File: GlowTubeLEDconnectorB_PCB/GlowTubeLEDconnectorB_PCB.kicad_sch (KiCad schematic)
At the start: 2 parts, among them U1 Contact pads, U2 Contact pads

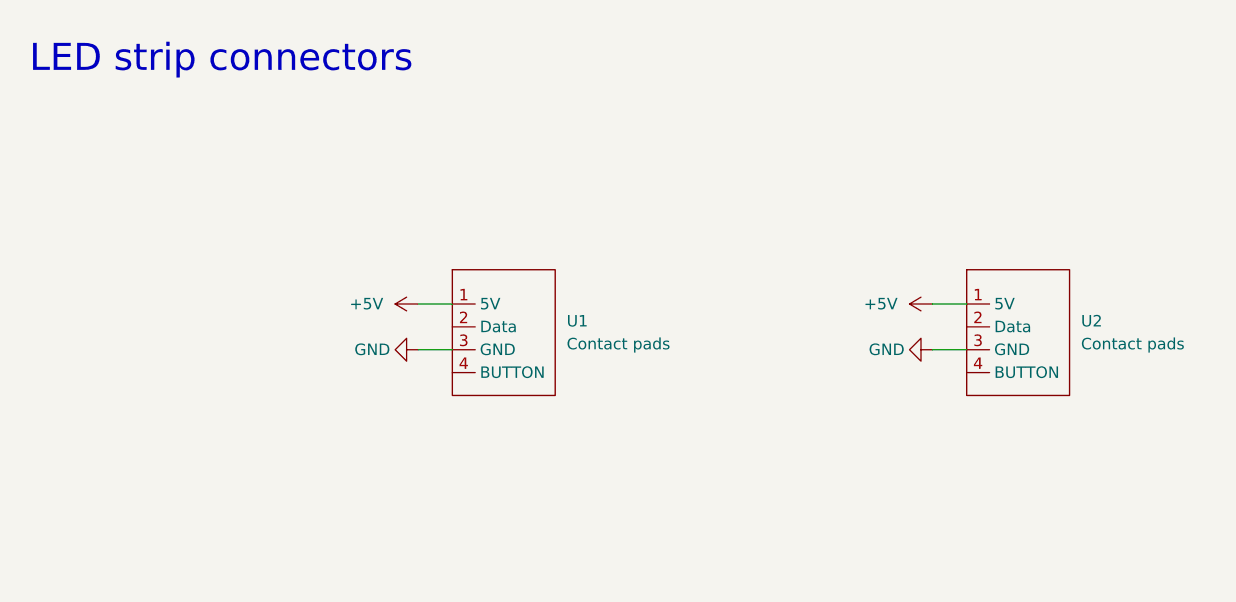
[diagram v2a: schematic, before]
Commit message: updated PCB designs to release candidate 1
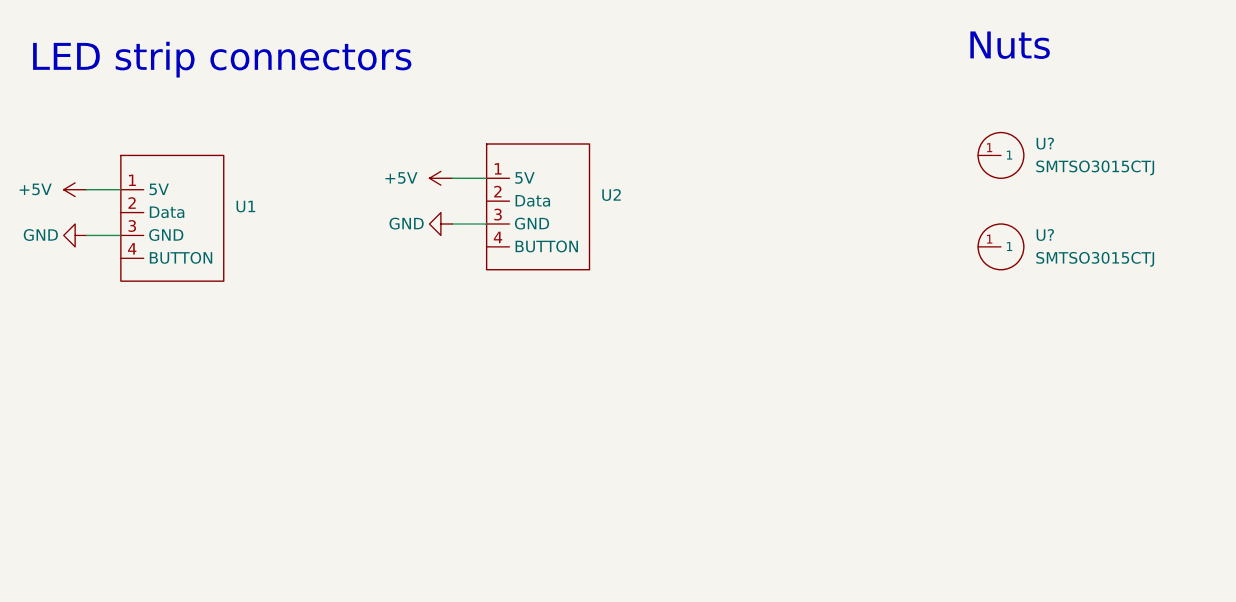
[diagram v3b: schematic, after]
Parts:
- added U? (x2): SMTSO3015CTJ, footprint:SMTSO3030CTJ, symbol MyParts:SMTSO3015CTJ
- U1, U2: value Contact pads -> (none); footprint myparts:LED strip connector 4pad small -> (none); now left out of the parts list
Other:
- note added: "Nuts"
- moved on the sheet: U1, U2
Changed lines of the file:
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@@
 (kicad_sch (version 20211123) (generator eeschema)
   (paper "A5")
-  (wire (pts (xy 64.77 52.07) (xy 68.58 52.07))
+  (wire (pts (xy 27.94 39.37) (xy 31.75 39.37))
     (stroke (width 0) (type default) (color 0 0 0 0))
   )
-  (wire (pts (xy 121.92 57.15) (xy 125.73 57.15))
+  (wire (pts (xy 68.58 43.18) (xy 72.39 43.18))
     (stroke (width 0) (type default) (color 0 0 0 0))
   )
-  (wire (pts (xy 121.92 52.07) (xy 125.73 52.07))
+  (wire (pts (xy 68.58 38.1) (xy 72.39 38.1))
     (stroke (width 0) (type default) (color 0 0 0 0))
   )
-  (wire (pts (xy 64.77 57.15) (xy 68.58 57.15))
+  (wire (pts (xy 27.94 44.45) (xy 31.75 44.45))
     (stroke (width 0) (type default) (color 0 0 0 0))
+  )
+  (text "Nuts" (at 125.73 25.4 0)
+    (effects (font (size 3 3)) (justify left bottom))
   )
   (text "LED strip connectors" (at 21.59 26.67 0)
     (effects (font (size 3 3)) (justify left bottom))
   )
-  (symbol (lib_id "myparts:LED_strip_contact_4pads") (at 72.39 52.07 0) (unit 1)
-    (in_bom yes) (on_board yes) (fields_autoplaced)
-    (property "Reference" "U1" (id 0) (at 81.28 53.9749 0)
+  (symbol (lib_id "myparts:LED_strip_contact_4pads") (at 35.56 39.37 0) (unit 1)
+    (in_bom no) (on_board yes) (fields_autoplaced)
+    (property "Reference" "U1" (id 0) (at 44.45 41.2749 0)
       (effects (font (size 1.27 1.27)) (justify left))
     )
-    (property "Value" "Contact pads" (id 1) (at 81.28 56.5149 0)
+    (property "Value" "" (id 1) (at 44.45 43.8149 0)
       (effects (font (size 1.27 1.27)) (justify left))
     )
-    (property "Footprint" "myparts:LED strip connector 4pad small" (id 2) (at 72.39 52.07 0)
+    (property "Footprint" "" (id 2) (at 35.56 39.37 0)
       (effects (font (size 1.27 1.27)) hide)
     )
-    (property "Datasheet" "" (id 3) (at 72.39 52.07 0)
+    (property "Datasheet" "" (id 3) (at 35.56 39.37 0)
       (effects (font (size 1.27 1.27)) hide)
     )
@@
     (pin "4")
   )
-  (symbol (lib_id "power:GND") (at 121.92 57.15 270) (unit 1)
-    (in_bom yes) (on_board yes)
-    (property "Reference" "#PWR0103" (id 0) (at 115.57 57.15 0)
-      (effects (font (size 1.27 1.27)) hide)
+  (symbol (lib_id "MyParts:SMTSO3015CTJ") (at 129.54 39.37 0) (unit 1)
+    (in_bom yes) (on_board yes) (fields_autoplaced)
+    (property "Reference" "U?" (id 0) (at 133.35 44.4499 0)
+      (effects (font (size 1.27 1.27)) (justify left))
     )
-    (property "Value" "GND" (id 1) (at 116.84 57.15 90))
-    (property "Footprint" "" (id 2) (at 121.92 57.15 0)
-      (effects (font (size 1.27 1.27)) hide)
+    (property "Value" "SMTSO3015CTJ" (id 1) (at 133.35 46.9899 0)
+      (effects (font (size 1.27 1.27)) (justify left))
     )
-    (property "Datasheet" "" (id 3) (at 121.92 57.15 0)
+    (property "Footprint" "footprint:SMTSO3030CTJ" (id 2) (at 129.54 49.53 0)
+      (effects (font (size 1.27 1.27) italic) hide)
+    )
+    (property "Datasheet" "https://img.jlc.com/pdf/applyPasteComponent/2021-07-26/212394W/84600014a36a49d2b26ab413315c8aa0/SINHOO%E7%94%B5%E8%B7%AF%E6%9D%BF%E8%A1%A8%E8%B4%B4%E8%9E%BA%E6%AF%8D%E6%9F%B1PCBSMDNuts.pdf" (id 3) (at 127.254 39.243 0)
+      (effects (font (size 1.27 1.27)) (justify left) hide)
+    )
+    (property "LCSC #" "C2915308" (id 4) (at 129.54 39.37 0)
       (effects (font (size 1.27 1.27)) hide)
     )
     (pin "1")
   )
-  (symbol (lib_id "power:+5V") (at 121.92 52.07 90) (unit 1)
+  (symbol (lib_id "power:GND") (at 68.58 43.18 270) (unit 1)
     (in_bom yes) (on_board yes)
-    (property "Reference" "#PWR0104" (id 0) (at 125.73 52.07 0)
+    (property "Reference" "#PWR0103" (id 0) (at 62.23 43.18 0)
       (effects (font (size 1.27 1.27)) hide)
     )
-    (property "Value" "+5V" (id 1) (at 114.3 52.07 90)
-      (effects (font (size 1.27 1.27)) (justify right))
-    )
-    (property "Footprint" "" (id 2) (at 121.92 52.07 0)
+    (property "Value" "GND" (id 1) (at 63.5 43.18 90))
+    (property "Footprint" "" (id 2) (at 68.58 43.18 0)
       (effects (font (size 1.27 1.27)) hide)
     )
-    (property "Datasheet" "" (id 3) (at 121.92 52.07 0)
+    (property "Datasheet" "" (id 3) (at 68.58 43.18 0)
       (effects (font (size 1.27 1.27)) hide)
     )
     (pin "1")
   )
-  (symbol (lib_id "myparts:LED_strip_contact_4pads") (at 129.54 52.07 0) (unit 1)
-    (in_bom yes) (on_board yes) (fields_autoplaced)
-    (property "Reference" "U2" (id 0) (at 138.43 53.9749 0)
+  (symbol (lib_id "power:+5V") (at 68.58 38.1 90) (unit 1)
+    (in_bom yes) (on_board yes)
+    (property "Reference" "#PWR0104" (id 0) (at 72.39 38.1 0)
+      (effects (font (size 1.27 1.27)) hide)
+    )
+    (property "Value" "+5V" (id 1) (at 60.96 38.1 90)
+      (effects (font (size 1.27 1.27)) (justify right))
+    )
+    (property "Footprint" "" (id 2) (at 68.58 38.1 0)
+      (effects (font (size 1.27 1.27)) hide)
+    )
+    (property "Datasheet" "" (id 3) (at 68.58 38.1 0)
+      (effects (font (size 1.27 1.27)) hide)
+    )
+    (pin "1")
+  )
+  (symbol (lib_id "myparts:LED_strip_contact_4pads") (at 76.2 38.1 0) (unit 1)
+    (in_bom no) (on_board yes) (fields_autoplaced)
+    (property "Reference" "U2" (id 0) (at 85.09 40.0049 0)
       (effects (font (size 1.27 1.27)) (justify left))
     )
-    (property "Value" "Contact pads" (id 1) (at 138.43 56.5149 0)
+    (property "Value" "" (id 1) (at 85.09 42.5449 0)
       (effects (font (size 1.27 1.27)) (justify left))
     )
-    (property "Footprint" "myparts:LED strip connector 4pad small" (id 2) (at 129.54 52.07 0)
+    (property "Footprint" "" (id 2) (at 76.2 38.1 0)
       (effects (font (size 1.27 1.27)) hide)
     )
-    (property "Datasheet" "" (id 3) (at 129.54 52.07 0)
+    (property "Datasheet" "" (id 3) (at 76.2 38.1 0)
       (effects (font (size 1.27 1.27)) hide)
     )
@@
     (pin "4")
   )
-  (symbol (lib_id "power:GND") (at 64.77 57.15 270) (unit 1)
-    (in_bom yes) (on_board yes)
-    (property "Reference" "#PWR0102" (id 0) (at 58.42 57.15 0)
-      (effects (font (size 1.27 1.27)) hide)
+  (symbol (lib_id "MyParts:SMTSO3015CTJ") (at 129.54 29.21 0) (unit 1)
+    (in_bom yes) (on_board yes) (fields_autoplaced)
+    (property "Reference" "U?" (id 0) (at 133.35 34.2899 0)
+      (effects (font (size 1.27 1.27)) (justify left))
     )
-    (property "Value" "GND" (id 1) (at 59.69 57.15 90))
-    (property "Footprint" "" (id 2) (at 64.77 57.15 0)
-      (effects (font (size 1.27 1.27)) hide)
+    (property "Value" "SMTSO3015CTJ" (id 1) (at 133.35 36.8299 0)
+      (effects (font (size 1.27 1.27)) (justify left))
     )
-    (property "Datasheet" "" (id 3) (at 64.77 57.15 0)
+    (property "Footprint" "footprint:SMTSO3030CTJ" (id 2) (at 129.54 39.37 0)
+      (effects (font (size 1.27 1.27) italic) hide)
+    )
+    (property "Datasheet" "https://img.jlc.com/pdf/applyPasteComponent/2021-07-26/212394W/84600014a36a49d2b26ab413315c8aa0/SINHOO%E7%94%B5%E8%B7%AF%E6%9D%BF%E8%A1%A8%E8%B4%B4%E8%9E%BA%E6%AF%8D%E6%9F%B1PCBSMDNuts.pdf" (id 3) (at 127.254 29.083 0)
+      (effects (font (size 1.27 1.27)) (justify left) hide)
+    )
+    (property "LCSC #" "C2915308" (id 4) (at 129.54 29.21 0)
       (effects (font (size 1.27 1.27)) hide)
     )
     (pin "1")
   )
-  (symbol (lib_id "power:+5V") (at 64.77 52.07 90) (unit 1)
+  (symbol (lib_id "power:GND") (at 27.94 44.45 270) (unit 1)
     (in_bom yes) (on_board yes)
-    (property "Reference" "#PWR0101" (id 0) (at 68.58 52.07 0)
+    (property "Reference" "#PWR0102" (id 0) (at 21.59 44.45 0)
       (effects (font (size 1.27 1.27)) hide)
     )
-    (property "Value" "+5V" (id 1) (at 57.15 52.07 90)
+    (property "Value" "GND" (id 1) (at 22.86 44.45 90))
+    (property "Footprint" "" (id 2) (at 27.94 44.45 0)
+      (effects (font (size 1.27 1.27)) hide)
+    )
+    (property "Datasheet" "" (id 3) (at 27.94 44.45 0)
+      (effects (font (size 1.27 1.27)) hide)
+    )
+    (pin "1")
+  )
+  (symbol (lib_id "power:+5V") (at 27.94 39.37 90) (unit 1)
+    (in_bom yes) (on_board yes)
+    (property "Reference" "#PWR0101" (id 0) (at 31.75 39.37 0)
+      (effects (font (size 1.27 1.27)) hide)
+    )
+    (property "Value" "+5V" (id 1) (at 20.32 39.37 90)
       (effects (font (size 1.27 1.27)) (justify right))
     )
-    (property "Footprint" "" (id 2) (at 64.77 52.07 0)
+    (property "Footprint" "" (id 2) (at 27.94 39.37 0)
       (effects (font (size 1.27 1.27)) hide)
     )
-    (property "Datasheet" "" (id 3) (at 64.77 52.07 0)
+    (property "Datasheet" "" (id 3) (at 27.94 39.37 0)
       (effects (font (size 1.27 1.27)) hide)
     )
@@
       (reference "U2") (unit 1) (value "Contact pads") (footprint "myparts:LED strip connector 4pad small")
     )
+    (path "/39f69e4c-3d98-4642-8cee-de7f9bf86b5e"
+      (reference "U?") (unit 1) (value "SMTSO3015CTJ") (footprint "footprint:SMTSO3030CTJ")
+    )
+    (path "/b1bdb303-cb9b-4bc2-a172-da9546d29135"
+      (reference "U?") (unit 1) (value "SMTSO3015CTJ") (footprint "footprint:SMTSO3030CTJ")
+    )
   )
